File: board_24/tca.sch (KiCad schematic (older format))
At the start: 47 parts, among them IC1 ATMEGA328-A, P1 CONN_2, P2 CONN_3X2, P3 CONN_8X2, P4 CONN_8X2, P5 CONN_8X2, P6 CONN_8X2, P7 CONN_8X2, P8 CONN_8X2, Q1 BSS138, U1 TLC5941, U2 TLC5941, U3 TLC5941, U4 SD_CARD, U5 LD1117S50, U6 LD1117S33, Y1 RESONATEUR

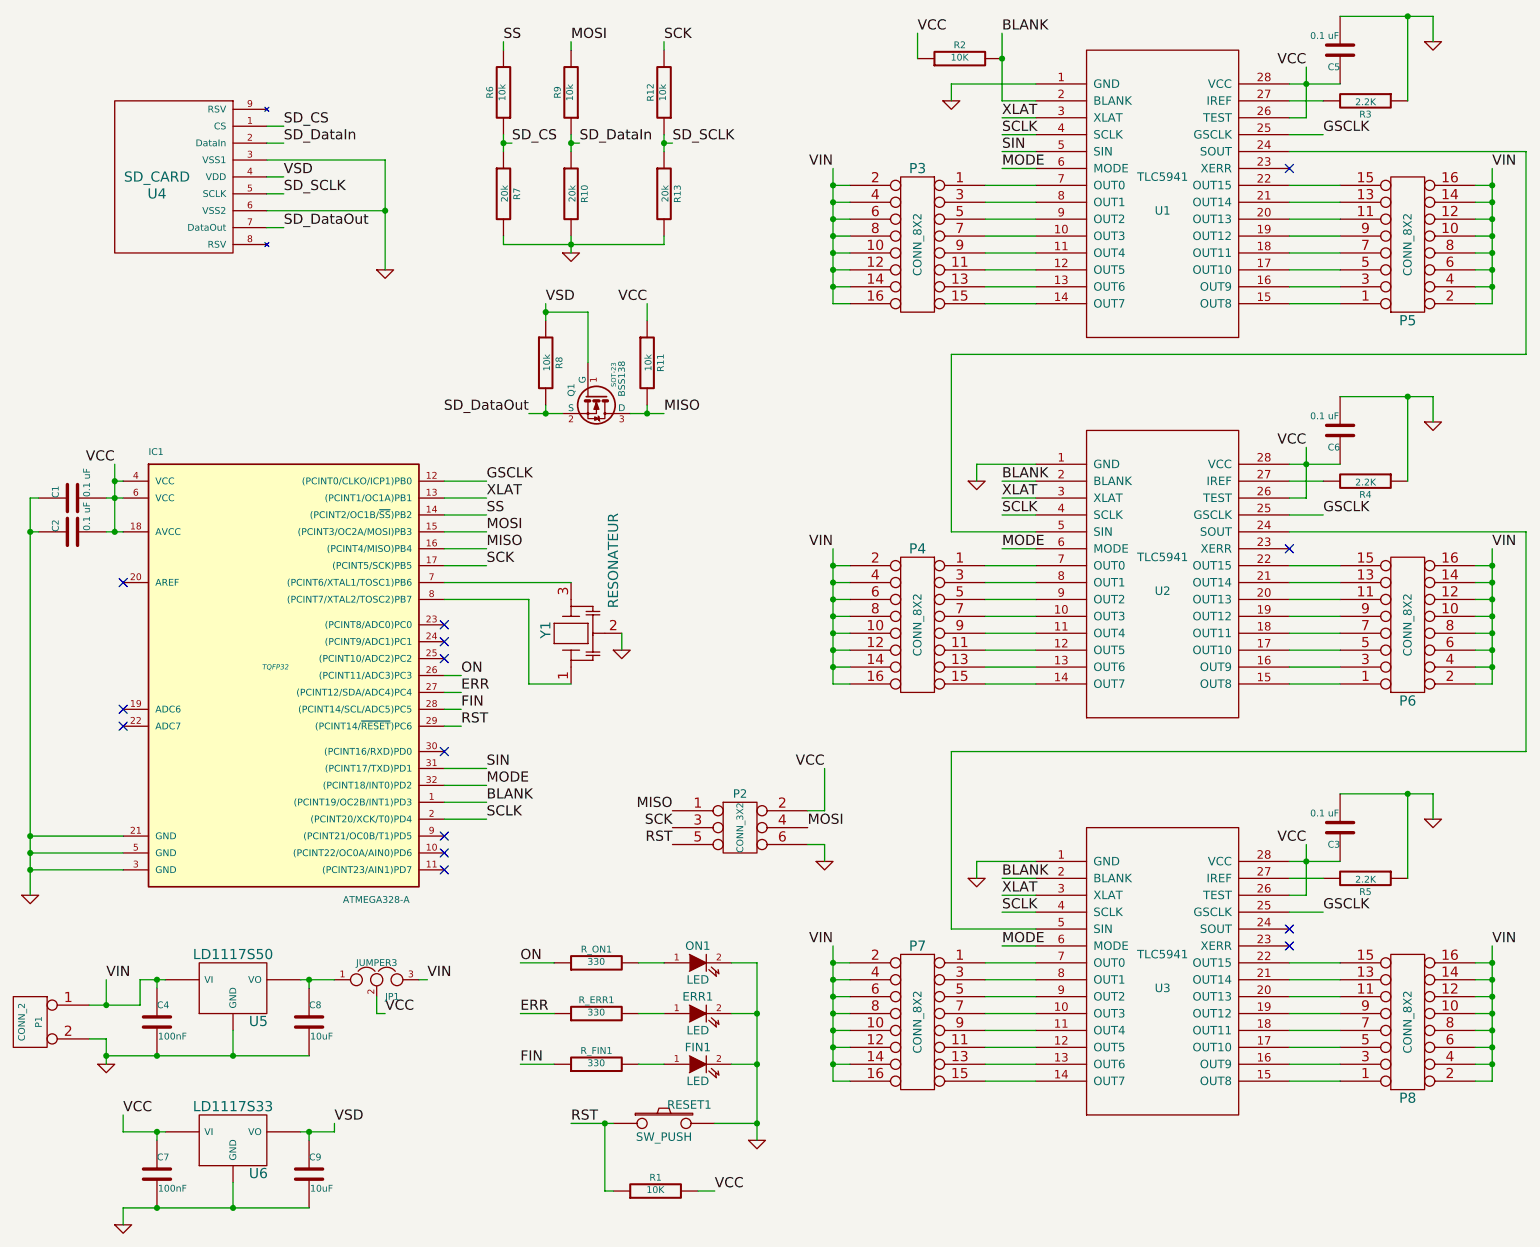
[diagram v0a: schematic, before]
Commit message: Eliminated duplicate board_24 folder.
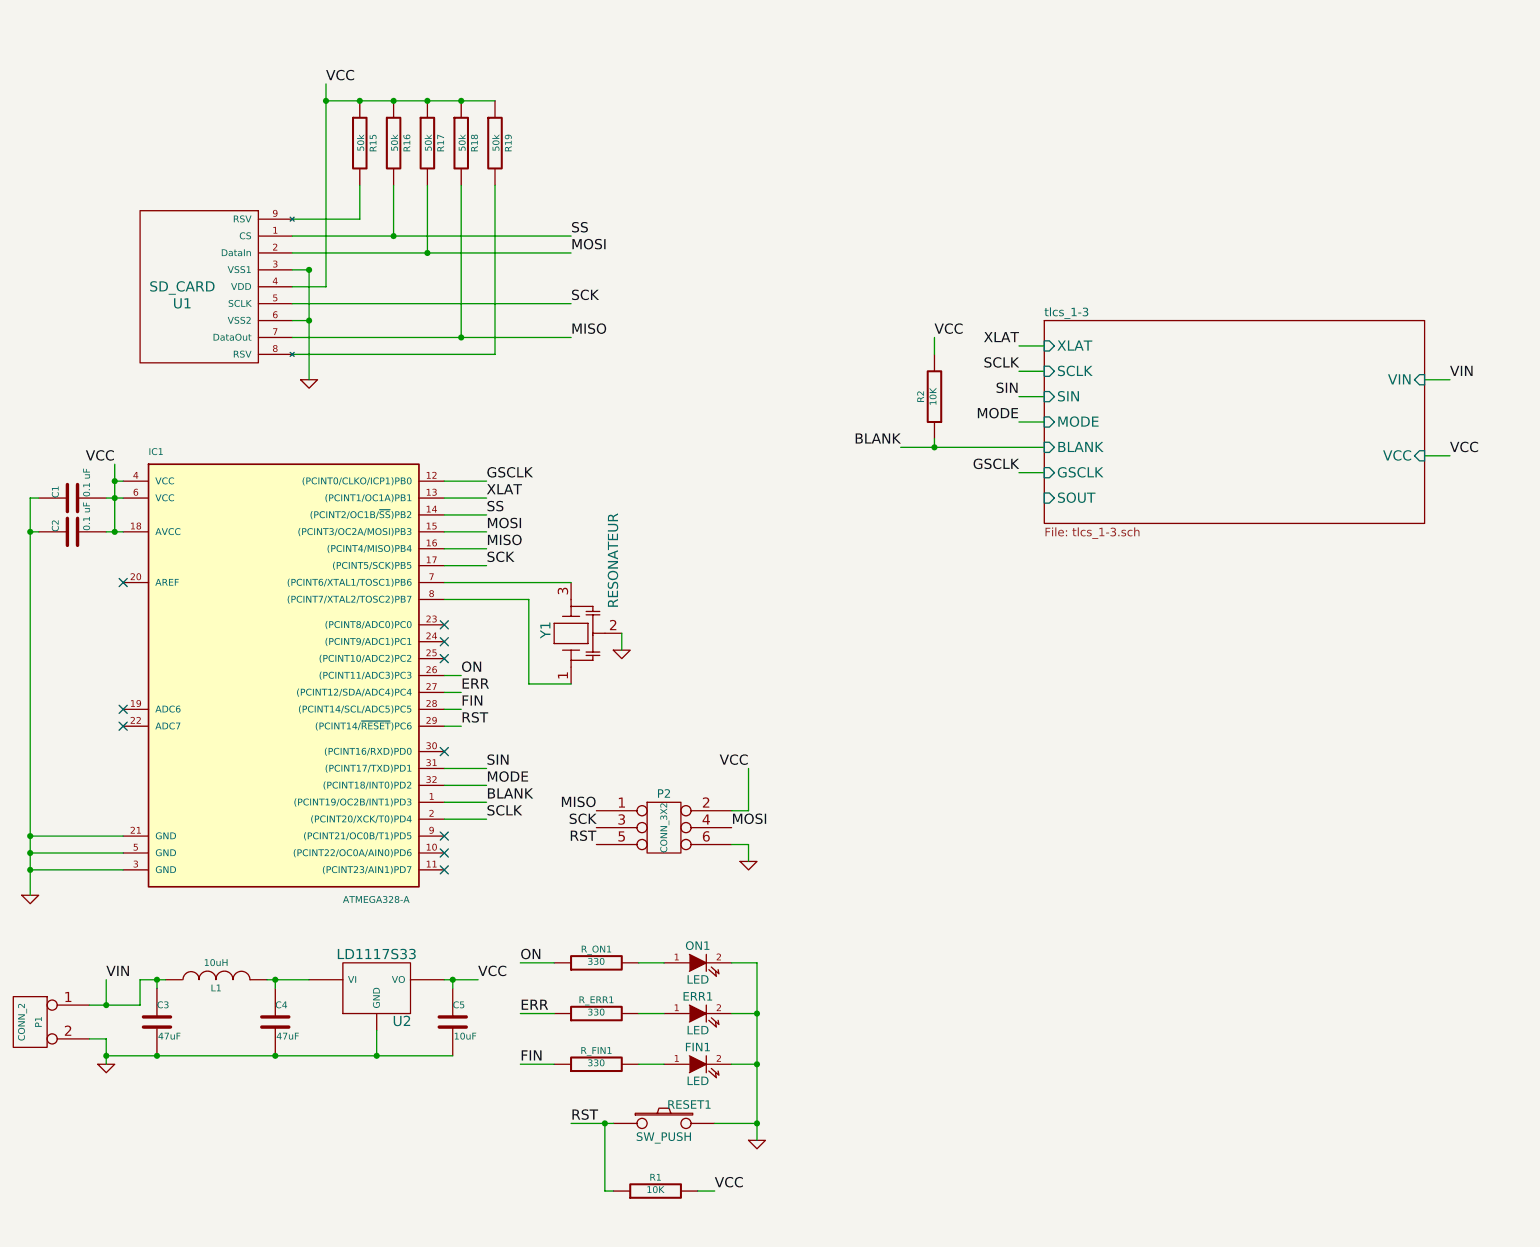
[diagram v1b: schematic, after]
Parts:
- removed C3, C5, C6: 0.1 uF, ~, symbol C
- removed C7: 100nF, ~, symbol C
- removed C9: 10uF, ~, symbol C
- removed JP1: JUMPER3, ~, symbol JUMPER3
- removed P3, P4, P5, P6, P7, P8: CONN_8X2, symbol CONN_8X2
- removed Q1: BSS138, SOT-23, symbol BSS138
- removed R10, R13, R7: 20k, ~, symbol R
- removed R11, R12, R6, R8, R9: 10k, ~, symbol R
- removed R3, R4, R5: 2.2K, ~, symbol R
- removed U1, U2, U3: TLC5941, MODULE, symbol TLC5941
- removed U6: LD1117S33, ~, symbol LD1117S33
- added C4: 47uF, c_elec_6.3x5.3, symbol C
- added L1: 10uH, SM1210, symbol INDUCTOR
- added R15, R16, R17, R18, R19: 50k, ~, symbol R
- C1, C2, ERR1, FIN1, ON1, R1, R2, R_ERR1, R_FIN1, R_ON1: footprint ~ -> SM0805
- C3: renamed from C4; value 100nF -> 47uF; footprint ~ -> c_elec_6.3x5.3
- C5: renamed from C8; footprint ~ -> SM0805
- IC1: footprint TQFP32 -> TQFP32_FIXED
- P1: footprint (none) -> PIN_ARRAY_2X1_3960um
- P2: footprint (none) -> pin_array_3x2
- RESET1: footprint ~ -> SW_PUSH_SMD
- U1: renamed from U4; footprint (none) -> SD_CONN
- U2: renamed from U5; value LD1117S50 -> LD1117S33; footprint ~ -> SOT223
- Y1: footprint (none) -> crystal_smd
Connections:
- net SD_CS is gone; now on net SS: U1.1 (CS)
- net SD_DataIn is gone; now on net MOSI: U1.2 (DataIn)
- net SD_DataOut is gone; now on net MISO: U1.7 (DataOut)
- net SD_SCLK is gone; now on net SCK: U1.5 (SCLK)
- net VSD is gone; now on net VCC: U1.4 (VDD)
- net BLANK: now also R2.1; no longer R2.2
- net GND: now also C4.2
- net MISO: now also R18.2
- net MOSI: now also R17.2
- net SS: now also R16.2
- net VCC: now also C5.1, R2.2, U2.2 (VO), R15.1, R16.1, R17.1, R18.1, R19.1; no longer R2.1
- net VIN: now also L1.1; no longer U2.3 (VI)
- net at U1.8 (RSV): now also R19.2
- net at U1.9 (RSV): now also R15.2
- new net: C4.1, L1.2, U2.3 (VI)
- no-connect marks 14 -> 10
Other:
- moved on the sheet: C5, P2, U1, U2
